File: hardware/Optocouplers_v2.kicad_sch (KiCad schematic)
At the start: 7 parts

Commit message: changed some footprints for clarity, and made some progress on board
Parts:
- removed U?: FOD8802DR2, SOIC127P600X175-8N, symbol FOD8802DR2:FOD8802DR2
- added O3: FOD8802DR2_IMG, FOD8802DR2:SOIC127P600X175-8N, symbol FOD8802DR2:FOD8802DR2_IMG
- gave numbers to parts that had none: 6
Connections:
- net +3V3: now also O3.6, O3.8
- net GND: now also O3.2, O3.4
- net OUT_1: now also O3.7
- net OUT_2: now also O3.5
- net at D13.1 (K), R13.1: now also O3.1
- net at D14.1 (K), R14.1: now also O3.3
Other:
- moved on the sheet: D13, D14, R13, R14, R15, R16

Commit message: finished new wersion of the board
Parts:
- added R55: 10k, Resistor_SMD:R_0603_1608Metric, symbol Device:R_Small
- renumbered D13 to D1, D14 to D2, O3 to O1, R13 to R5, R14 to R6, R15 to R7, R16 to R8
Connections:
- net +3V3: now also R55.2; no longer O1.6, O1.8
- new net: O1.6, O1.8, R55.1
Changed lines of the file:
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@@
+    (stroke (width 0) (type default) (color 0 0 0 0))
+  )
+  (wire (pts (xy 157.48 71.755) (xy 157.48 74.295))
     (stroke (width 0) (type default) (color 0 0 0 0))
   )
@@
   (symbol (lib_id "Device:R_Small") (at 165.1 104.14 180)
     (in_bom yes) (on_board yes)
-    (property "Reference" "R16" (id 0) (at 170.18 104.14 90))
+    (property "Reference" "R8" (id 0) (at 170.18 104.14 90))
     (property "Value" "10k" (id 1) (at 167.64 104.14 90))
     (property "Footprint" "Resistor_SMD:R_0603_1608Metric" (id 2) (at 165.1 104.14 0)
@@
   (symbol (lib_id "FOD8802DR2:FOD8802DR2_IMG") (at 148.59 79.375 0)
     (in_bom yes) (on_board yes) (fields_autoplaced)
-    (property "Reference" "O3" (id 0) (at 147.32 77.47 0))
+    (property "Reference" "O1" (id 0) (at 147.32 77.47 0))
     (property "Value" "FOD8802DR2_IMG" (id 1) (at 147.32 80.01 0))
     (property "Footprint" "FOD8802DR2:SOIC127P600X175-8N" (id 2) (at 148.59 79.375 0)
@@
     (pin "8")
   )
-  (symbol (lib_id "power:+3.3V") (at 157.48 79.375 0)
-    (in_bom yes) (on_board yes) (fields_autoplaced)
-    (property "Reference" "#PWR0147" (id 0) (at 157.48 83.185 0)
-      (effects (font (size 1.27 1.27)) hide)
-    )
-    (property "Value" "+3.3V" (id 1) (at 157.48 74.295 0))
-    (property "Footprint" "" (id 2) (at 157.48 79.375 0)
-      (effects (font (size 1.27 1.27)) hide)
-    )
-    (property "Datasheet" "" (id 3) (at 157.48 79.375 0)
+  (symbol (lib_id "power:+3.3V") (at 157.48 71.755 0)
+    (in_bom yes) (on_board yes) (fields_autoplaced)
+    (property "Reference" "#PWR0147" (id 0) (at 157.48 75.565 0)
+      (effects (font (size 1.27 1.27)) hide)
+    )
+    (property "Value" "+3.3V" (id 1) (at 157.48 66.675 0))
+    (property "Footprint" "" (id 2) (at 157.48 71.755 0)
+      (effects (font (size 1.27 1.27)) hide)
+    )
+    (property "Datasheet" "" (id 3) (at 157.48 71.755 0)
       (effects (font (size 1.27 1.27)) hide)
     )
@@
   (symbol (lib_id "Device:R_Small") (at 160.02 104.14 180)
     (in_bom yes) (on_board yes)
-    (property "Reference" "R15" (id 0) (at 154.94 104.14 90))
+    (property "Reference" "R7" (id 0) (at 154.94 104.14 90))
     (property "Value" "10k" (id 1) (at 157.48 104.14 90))
     (property "Footprint" "Resistor_SMD:R_0603_1608Metric" (id 2) (at 160.02 104.14 0)
@@
   (symbol (lib_id "Device:R_Small") (at 120.65 84.455 270)
     (in_bom yes) (on_board yes) (fields_autoplaced)
-    (property "Reference" "R13" (id 0) (at 120.65 78.105 90))
+    (property "Reference" "R5" (id 0) (at 120.65 78.105 90))
     (property "Value" "--" (id 1) (at 120.65 80.645 90))
     (property "Footprint" "Resistor_SMD:R_0603_1608Metric" (id 2) (at 120.65 84.455 0)
@@
   (symbol (lib_id "Device:R_Small") (at 120.65 93.345 270)
     (in_bom yes) (on_board yes)
-    (property "Reference" "R14" (id 0) (at 120.65 100.965 90))
+    (property "Reference" "R6" (id 0) (at 120.65 100.965 90))
     (property "Value" "--" (id 1) (at 120.65 98.425 90))
     (property "Footprint" "Resistor_SMD:R_0603_1608Metric" (id 2) (at 120.65 93.345 0)
@@
   (symbol (lib_id "Device:D_Schottky_Small") (at 132.08 100.965 270)
     (in_bom yes) (on_board yes)
-    (property "Reference" "D14" (id 0) (at 133.858 100.965 90)
+    (property "Reference" "D2" (id 0) (at 133.858 100.965 90)
       (effects (font (size 1.27 1.27)) (justify left))
     )
@@
   (symbol (lib_id "Device:D_Schottky_Small") (at 126.365 100.965 270)
     (in_bom yes) (on_board yes)
-    (property "Reference" "D13" (id 0) (at 128.143 100.965 90)
+    (property "Reference" "D1" (id 0) (at 128.143 100.965 90)
       (effects (font (size 1.27 1.27)) (justify left))
     )
@@
       (effects (font (size 1.27 1.27)) hide)
     )
+    (pin "1")
+    (pin "2")
+  )
+  (symbol (lib_id "Device:R_Small") (at 157.48 76.835 180)
+    (in_bom yes) (on_board yes)
+    (property "Reference" "R55" (id 0) (at 152.4 76.835 90))
+    (property "Value" "10k" (id 1) (at 154.94 76.835 90))
+    (property "Footprint" "Resistor_SMD:R_0603_1608Metric" (id 2) (at 157.48 76.835 0)
+      (effects (font (size 1.27 1.27)) hide)
+    )
+    (property "Datasheet" "~" (id 3) (at 157.48 76.835 0)
+      (effects (font (size 1.27 1.27)) hide)
+    )

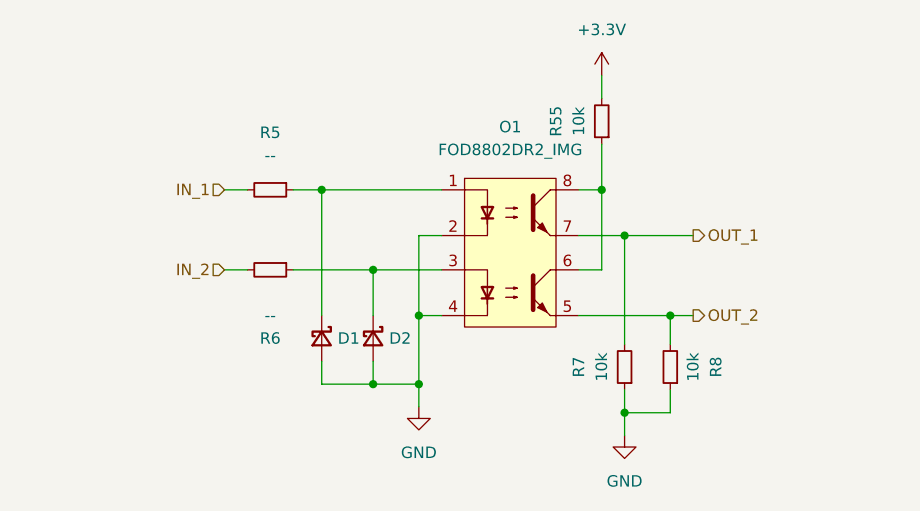
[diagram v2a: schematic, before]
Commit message: debuged the board, changed one opto for mosfet, changed the way water and potentiometers were supplied. Also standrised opamps (yoinked opamps from data Data_Acquisition_Cards)
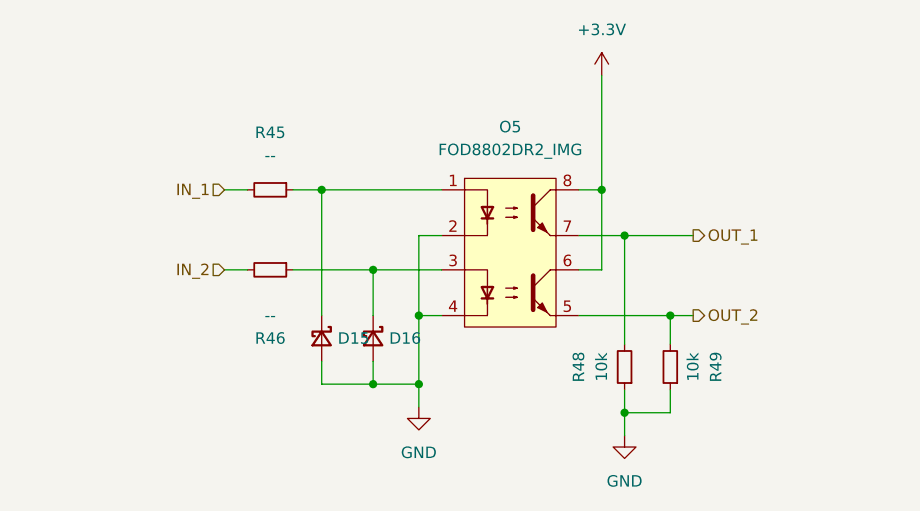
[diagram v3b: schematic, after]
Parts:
- removed R55: 10k, Resistor_SMD:R_0603_1608Metric, symbol Device:R_Small
- renumbered D1 to D15, D2 to D16, O1 to O5, R5 to R45, R6 to R46, R7 to R48, R8 to R49
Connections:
- net +3V3: now also O5.6, O5.8
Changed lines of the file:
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@@
-    (stroke (width 0) (type default) (color 0 0 0 0))
-  )
-  (wire (pts (xy 157.48 79.375) (xy 157.48 84.455))
     (stroke (width 0) (type default) (color 0 0 0 0))
   )
@@
     (stroke (width 0) (type default) (color 0 0 0 0))
   )
-  (wire (pts (xy 157.48 71.755) (xy 157.48 74.295))
+  (wire (pts (xy 157.48 71.755) (xy 157.48 84.455))
     (stroke (width 0) (type default) (color 0 0 0 0))
   )
@@
   (symbol (lib_id "Device:R_Small") (at 165.1 104.14 180)
     (in_bom yes) (on_board yes)
-    (property "Reference" "R8" (id 0) (at 170.18 104.14 90))
+    (property "Reference" "R49" (id 0) (at 170.18 104.14 90))
     (property "Value" "10k" (id 1) (at 167.64 104.14 90))
     (property "Footprint" "Resistor_SMD:R_0603_1608Metric" (id 2) (at 165.1 104.14 0)
@@
   (symbol (lib_id "FOD8802DR2:FOD8802DR2_IMG") (at 148.59 79.375 0)
     (in_bom yes) (on_board yes) (fields_autoplaced)
-    (property "Reference" "O1" (id 0) (at 147.32 77.47 0))
+    (property "Reference" "O5" (id 0) (at 147.32 77.47 0))
     (property "Value" "FOD8802DR2_IMG" (id 1) (at 147.32 80.01 0))
     (property "Footprint" "FOD8802DR2:SOIC127P600X175-8N" (id 2) (at 148.59 79.375 0)
@@
   (symbol (lib_id "Device:R_Small") (at 160.02 104.14 180)
     (in_bom yes) (on_board yes)
-    (property "Reference" "R7" (id 0) (at 154.94 104.14 90))
+    (property "Reference" "R48" (id 0) (at 154.94 104.14 90))
     (property "Value" "10k" (id 1) (at 157.48 104.14 90))
     (property "Footprint" "Resistor_SMD:R_0603_1608Metric" (id 2) (at 160.02 104.14 0)
@@
   (symbol (lib_id "Device:R_Small") (at 120.65 84.455 270)
     (in_bom yes) (on_board yes) (fields_autoplaced)
-    (property "Reference" "R5" (id 0) (at 120.65 78.105 90))
+    (property "Reference" "R45" (id 0) (at 120.65 78.105 90))
     (property "Value" "--" (id 1) (at 120.65 80.645 90))
     (property "Footprint" "Resistor_SMD:R_0603_1608Metric" (id 2) (at 120.65 84.455 0)
@@
   (symbol (lib_id "Device:R_Small") (at 120.65 93.345 270)
     (in_bom yes) (on_board yes)
-    (property "Reference" "R6" (id 0) (at 120.65 100.965 90))
+    (property "Reference" "R46" (id 0) (at 120.65 100.965 90))
     (property "Value" "--" (id 1) (at 120.65 98.425 90))
     (property "Footprint" "Resistor_SMD:R_0603_1608Metric" (id 2) (at 120.65 93.345 0)
@@
   (symbol (lib_id "Device:D_Schottky_Small") (at 132.08 100.965 270)
     (in_bom yes) (on_board yes)
-    (property "Reference" "D2" (id 0) (at 133.858 100.965 90)
+    (property "Reference" "D16" (id 0) (at 133.858 100.965 90)
       (effects (font (size 1.27 1.27)) (justify left))
     )
@@
   (symbol (lib_id "Device:D_Schottky_Small") (at 126.365 100.965 270)
     (in_bom yes) (on_board yes)
-    (property "Reference" "D1" (id 0) (at 128.143 100.965 90)
+    (property "Reference" "D15" (id 0) (at 128.143 100.965 90)
       (effects (font (size 1.27 1.27)) (justify left))
     )
@@
       (effects (font (size 1.27 1.27)) hide)
     )
-    (pin "1")
-    (pin "2")
-  )
-  (symbol (lib_id "Device:R_Small") (at 157.48 76.835 180)
-    (in_bom yes) (on_board yes)
-    (property "Reference" "R55" (id 0) (at 152.4 76.835 90))
-    (property "Value" "10k" (id 1) (at 154.94 76.835 90))
-    (property "Footprint" "Resistor_SMD:R_0603_1608Metric" (id 2) (at 157.48 76.835 0)
-      (effects (font (size 1.27 1.27)) hide)
-    )
-    (property "Datasheet" "~" (id 3) (at 157.48 76.835 0)
-      (effects (font (size 1.27 1.27)) hide)
-    )

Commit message: nameing scheme update
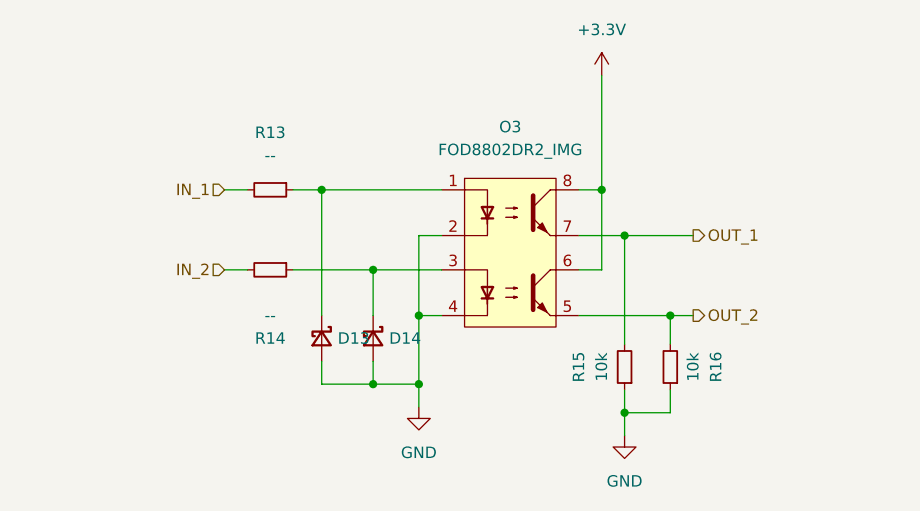
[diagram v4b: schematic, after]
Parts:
- renumbered D15 to D13, D16 to D14, O5 to O3, R45 to R13, R46 to R14, R48 to R15, R49 to R16
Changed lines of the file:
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@@
   (symbol (lib_id "power:GND") (at 160.02 111.76 0)
     (in_bom yes) (on_board yes) (fields_autoplaced)
-    (property "Reference" "#PWR0148" (id 0) (at 160.02 118.11 0)
+    (property "Reference" "#PWR0145" (id 0) (at 160.02 118.11 0)
       (effects (font (size 1.27 1.27)) hide)
     )
@@
   (symbol (lib_id "Device:R_Small") (at 165.1 104.14 180)
     (in_bom yes) (on_board yes)
-    (property "Reference" "R49" (id 0) (at 170.18 104.14 90))
+    (property "Reference" "R16" (id 0) (at 170.18 104.14 90))
     (property "Value" "10k" (id 1) (at 167.64 104.14 90))
     (property "Footprint" "Resistor_SMD:R_0603_1608Metric" (id 2) (at 165.1 104.14 0)
@@
   (symbol (lib_id "FOD8802DR2:FOD8802DR2_IMG") (at 148.59 79.375 0)
     (in_bom yes) (on_board yes) (fields_autoplaced)
-    (property "Reference" "O5" (id 0) (at 147.32 77.47 0))
+    (property "Reference" "O3" (id 0) (at 147.32 77.47 0))
     (property "Value" "FOD8802DR2_IMG" (id 1) (at 147.32 80.01 0))
     (property "Footprint" "FOD8802DR2:SOIC127P600X175-8N" (id 2) (at 148.59 79.375 0)
@@
   (symbol (lib_id "power:+3.3V") (at 157.48 71.755 0)
     (in_bom yes) (on_board yes) (fields_autoplaced)
-    (property "Reference" "#PWR0147" (id 0) (at 157.48 75.565 0)
+    (property "Reference" "#PWR0144" (id 0) (at 157.48 75.565 0)
       (effects (font (size 1.27 1.27)) hide)
     )
@@
   (symbol (lib_id "Device:R_Small") (at 160.02 104.14 180)
     (in_bom yes) (on_board yes)
-    (property "Reference" "R48" (id 0) (at 154.94 104.14 90))
+    (property "Reference" "R15" (id 0) (at 154.94 104.14 90))
     (property "Value" "10k" (id 1) (at 157.48 104.14 90))
     (property "Footprint" "Resistor_SMD:R_0603_1608Metric" (id 2) (at 160.02 104.14 0)
@@
   (symbol (lib_id "Device:R_Small") (at 120.65 84.455 270)
     (in_bom yes) (on_board yes) (fields_autoplaced)
-    (property "Reference" "R45" (id 0) (at 120.65 78.105 90))
+    (property "Reference" "R13" (id 0) (at 120.65 78.105 90))
     (property "Value" "--" (id 1) (at 120.65 80.645 90))
     (property "Footprint" "Resistor_SMD:R_0603_1608Metric" (id 2) (at 120.65 84.455 0)
@@
   (symbol (lib_id "Device:R_Small") (at 120.65 93.345 270)
     (in_bom yes) (on_board yes)
-    (property "Reference" "R46" (id 0) (at 120.65 100.965 90))
+    (property "Reference" "R14" (id 0) (at 120.65 100.965 90))
     (property "Value" "--" (id 1) (at 120.65 98.425 90))
     (property "Footprint" "Resistor_SMD:R_0603_1608Metric" (id 2) (at 120.65 93.345 0)
@@
   (symbol (lib_id "power:GND") (at 137.16 108.585 0)
     (in_bom yes) (on_board yes) (fields_autoplaced)
-    (property "Reference" "#PWR0149" (id 0) (at 137.16 114.935 0)
+    (property "Reference" "#PWR0146" (id 0) (at 137.16 114.935 0)
       (effects (font (size 1.27 1.27)) hide)
     )
@@
   (symbol (lib_id "Device:D_Schottky_Small") (at 132.08 100.965 270)
     (in_bom yes) (on_board yes)
-    (property "Reference" "D16" (id 0) (at 133.858 100.965 90)
+    (property "Reference" "D14" (id 0) (at 133.858 100.965 90)
       (effects (font (size 1.27 1.27)) (justify left))
     )
@@
   (symbol (lib_id "Device:D_Schottky_Small") (at 126.365 100.965 270)
     (in_bom yes) (on_board yes)
-    (property "Reference" "D15" (id 0) (at 128.143 100.965 90)
+    (property "Reference" "D13" (id 0) (at 128.143 100.965 90)
       (effects (font (size 1.27 1.27)) (justify left))
     )
